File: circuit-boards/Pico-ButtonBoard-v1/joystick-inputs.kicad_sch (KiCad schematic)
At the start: 26 parts, among them J20 XY0-R, J21 XY1-L, U6 SN74LVC1G3157DBVR, U8 TLV77033DDC

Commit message: Update footprints
Signed-off-by: Scott Berman <sgberman1@gmail.com>
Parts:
- added TP301, TP302: CAN_RX, TestPoint:TestPoint_Keystone_5000-5004_Miniature, symbol Connector:TestPoint
- C301: renamed from C33; DIST (none) -> Digikey; DIST P/N (none) -> 445-4116-1-ND; MFG (none) -> TDK; MFG P/N (none) -> C2012X5R1E475K125AB
- C302: renamed from C27; value 1000pF-50V-10%-0805 -> 1000pF-50V-5%-0805; DIST (none) -> Digikey; DIST P/N (none) -> 399-C0805C102J5GACTUCT-ND; MFG (none) -> KEMET; MFG P/N (none) -> C0805C102J5GACTU
- C303: renamed from C25; value 1000pF-50V-10%-0805 -> 1000pF-50V-5%-0805; DIST (none) -> Digikey; DIST P/N (none) -> 399-C0805C102J5GACTUCT-ND; MFG (none) -> KEMET; MFG P/N (none) -> C0805C102J5GACTU
- C304: renamed from C28; value 1000pF-50V-10%-0805 -> 1000pF-50V-5%-0805; DIST (none) -> Digikey; DIST P/N (none) -> 399-C0805C102J5GACTUCT-ND; MFG (none) -> KEMET; MFG P/N (none) -> C0805C102J5GACTU
- C305: renamed from C26; value 1000pF-50V-10%-0805 -> 1000pF-50V-5%-0805; DIST (none) -> Digikey; DIST P/N (none) -> 399-C0805C102J5GACTUCT-ND; MFG (none) -> KEMET; MFG P/N (none) -> C0805C102J5GACTU
- C306: renamed from C31; DIST (none) -> Digikey; DIST P/N (none) -> 445-4116-1-ND; MFG (none) -> TDK; MFG P/N (none) -> C2012X5R1E475K125AB
- C309: renamed from C30; DIST (none) -> Digikey; DIST P/N (none) -> 445-4116-1-ND; MFG (none) -> TDK; MFG P/N (none) -> C2012X5R1E475K125AB
- C311: renamed from C37; value 1000pF-50V-10%-0805 -> 1000pF-50V-5%-0805; DIST (none) -> Digikey; DIST P/N (none) -> 399-C0805C102J5GACTUCT-ND; MFG (none) -> KEMET; MFG P/N (none) -> C0805C102J5GACTU
- R301: renamed from R55; DIST (none) -> Digikey; DIST P/N (none) -> 311-100KCRCT-ND; MFG (none) -> YAGEO; MFG P/N (none) -> RC0805FR-07100KL
- R302: renamed from R54; DIST (none) -> Digikey; DIST P/N (none) -> 311-100KCRCT-ND; MFG (none) -> YAGEO; MFG P/N (none) -> RC0805FR-07100KL
- R303: renamed from R56; DIST (none) -> Digikey; DIST P/N (none) -> 311-100KCRCT-ND; MFG (none) -> YAGEO; MFG P/N (none) -> RC0805FR-07100KL
- R304: renamed from R53; DIST (none) -> Digikey; DIST P/N (none) -> 311-100KCRCT-ND; MFG (none) -> YAGEO; MFG P/N (none) -> RC0805FR-07100KL
- R305: renamed from R57; value 49R9-1%-0805 -> 49.9R-1%-0805; DIST P/N 311-1.50KCRCT-ND -> RMCF0805FT49R9CT-ND; MFG YAGEO -> Stackpole; MFG P/N RC0805FR-071K5L -> RMCF0805FT49R9
- R306: renamed from R58; value 49R9-1%-0805 -> 49.9R-1%-0805; DIST P/N 311-1.50KCRCT-ND -> RMCF0805FT49R9CT-ND; MFG YAGEO -> Stackpole; MFG P/N RC0805FR-071K5L -> RMCF0805FT49R9
- R307: renamed from R51; value 49R9-1%-0805 -> 49.9R-1%-0805; DIST P/N 311-1.50KCRCT-ND -> RMCF0805FT49R9CT-ND; MFG YAGEO -> Stackpole; MFG P/N RC0805FR-071K5L -> RMCF0805FT49R9
- R308: renamed from R52; value 49R9-1%-0805 -> 49.9R-1%-0805; DIST P/N 311-1.50KCRCT-ND -> RMCF0805FT49R9CT-ND; MFG YAGEO -> Stackpole; MFG P/N RC0805FR-071K5L -> RMCF0805FT49R9
- R309: renamed from R50; DIST (none) -> Digikey; DIST P/N (none) -> 541-10.0KCCT-ND; MFG (none) -> Vishay Dale; MFG P/N (none) -> CRCW080510K0FKEA
- renumbered C32 to C307, C24 to C308, C29 to C310, J21 to J301, J20 to J302, L1 to L301, L2 to L302, U8 to U301, U6 to U302
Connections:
- net +3V3A: now also TP301.1
- net GNDA: now also TP302.1
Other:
- title: (none) -> Pico Button Board

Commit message: Pico Button Board initial placement
Signed-off-by: Scott Berman <sgberman1@gmail.com>
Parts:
- C307, C308, C310: LCSC Part # C519981 -> (none)

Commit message: Pico Button Board initial pcb checkin
Signed-off-by: Scott Berman <sgberman1@gmail.com>
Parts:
- removed L302: 10uH-10%-500mA-0805, Inductor_SMD:L_0805_2012Metric_Pad1.05x1.20mm_HandSolder, symbol Device:L_Small
- renumbered C302 to C10, C305 to C11, C301 to C16, C306 to C17, C309 to C18, C310 to C19, C308 to C21, C311 to C6, C307 to C7, C304 to C8, C303 to C9, J301 to J26, J302 to J27, L301 to L2, R309 to R28, R305 to R36, R306 to R37, R307 to R38, R308 to R39, R301 to R40, R303 to R41, R302 to R42, R304 to R43, TP301 to TP6, TP302 to TP7, U302 to U7, U301 to U9

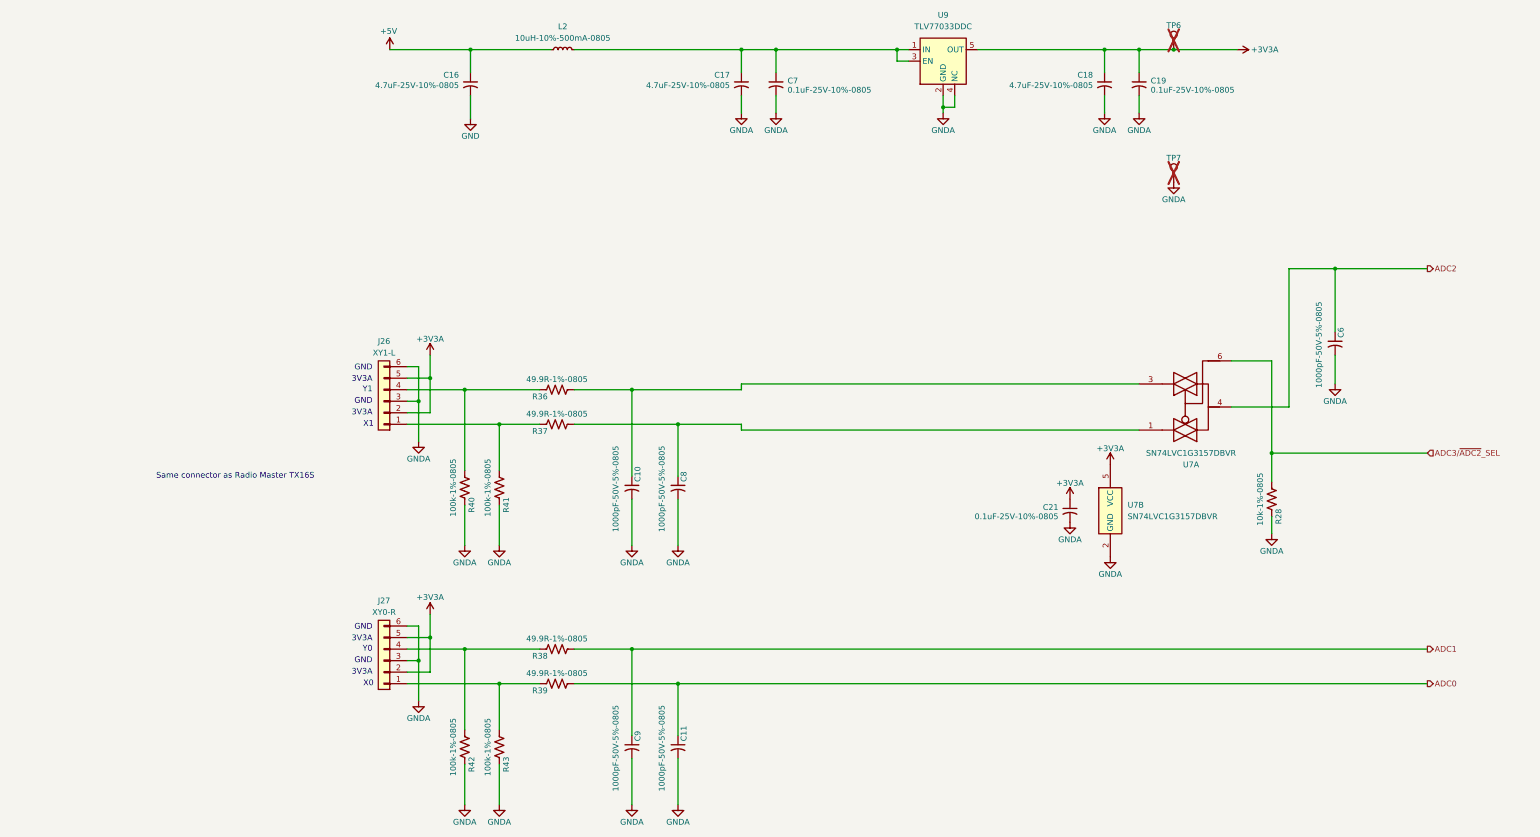
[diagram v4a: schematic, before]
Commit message: Changed button input circuit to use mux. Changed ADC3 to an external SPI ADC
Signed-off-by: Scott Berman <sgberman1@gmail.com>
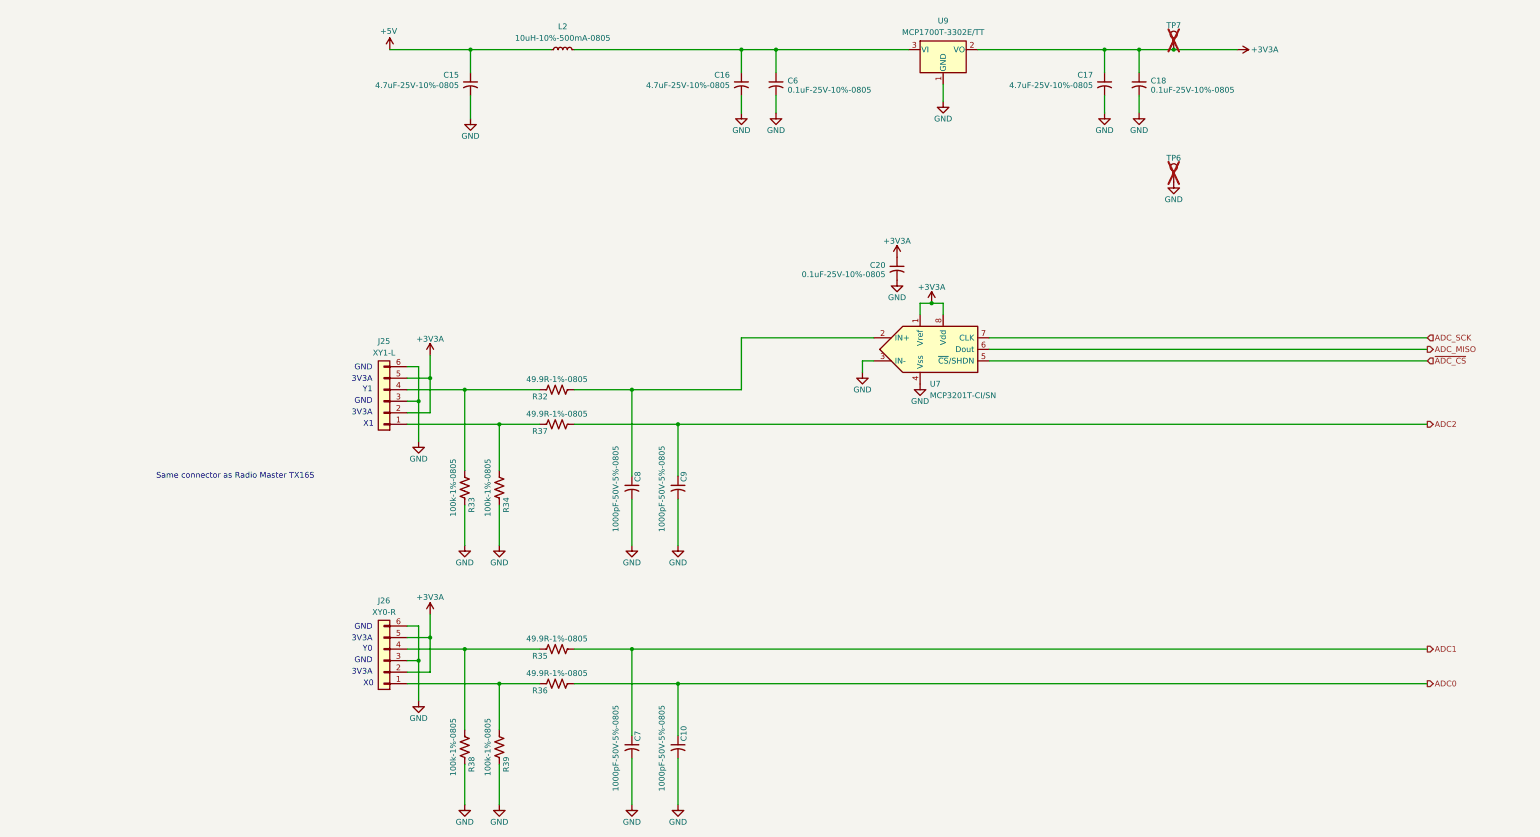
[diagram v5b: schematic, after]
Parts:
- removed C6: 1000pF-50V-5%-0805, Capacitor_SMD:C_0805_2012Metric_Pad1.18x1.45mm_HandSolder, symbol Device:C_Small_US
- removed R28: 10k-1%-0805, Resistor_SMD:R_0805_2012Metric_Pad1.20x1.40mm_HandSolder, symbol Device:R_US
- removed U7: SN74LVC1G3157DBVR, Package_TO_SOT_SMD:SOT-23-6_Handsoldering, symbol 74xGxx:74LVC1G3157
- removed U9: TLV77033DDC, Package_TO_SOT_SMD:SOT-23-5, symbol Pico-ButtonBoard:TLV77033DDC
- added U7: MCP3201T-CI/SN, Package_SO:SO-8_3.9x4.9mm_P1.27mm, symbol Analog_ADC:MCP3201
- added U9: MCP1700T-3302E/TT, Package_TO_SOT_SMD:SOT-23-3, symbol Regulator_Linear:MCP1700x-300xxTT
- renumbered C11 to C10, C16 to C15, C17 to C16, C18 to C17, C19 to C18, C21 to C20, C7 to C6, C9 to C7, C10 to C8, C8 to C9, J26 to J25, J27 to J26, R36 to R32, R40 to R33, R41 to R34, R38 to R35, R39 to R36, R42 to R38, R43 to R39, TP7 to TP6, TP6 to TP7
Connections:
- net GNDA is gone; now on net GND: C10.2, C16.2, C17.2, C18.2, C20.2, C6.2, C7.2, C8.2, C9.2, J25.3 (Pin_3), J25.6 (Pin_6), J26.3 (Pin_3), J26.6 (Pin_6), R33.1, R34.1, R38.1, R39.1, TP6.1
- net +3V3A: now also U7.1 (Vref), U7.8 (Vdd), U9.2 (VO)
- net ADC2: now also C9.1, R37.1
- net GND: now also U7.3 (IN-), U7.4 (Vss), U9.1 (GND)
- net at C16.1, C6.1, L2.2: now also U9.3 (VI)
- net at C8.1, R32.1: now also U7.2 (IN+)
- new net ADC_MISO: U7.6 (Dout)
- new net ADC_SCK: U7.7 (CLK)
- new net ~{ADC_CS}: U7.5 (~{CS}/SHDN)
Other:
- moved on the sheet: C20

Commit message: Add power over CAN to supply joystick from button interfaces.
Signed-off-by: Scott Berman <sgberman1@gmail.com>
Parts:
- TP4: renamed from TP6; value CAN_RX -> GND
- TP7: value CAN_RX -> 3V3A
- renumbered C15 to C13, C16 to C14, C17 to C15, C18 to C16, C20 to C18, C10 to C20, C9 to C21, C7 to C6, C8 to C7, C6 to C8, J26 to J25, J25 to J26, R35 to R24, R36 to R25, R37 to R26, R32 to R27, R38 to R45, R39 to R46, R34 to R47, R33 to R48
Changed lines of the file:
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@@
 	(title_block
 		(title "Pico Button Board")
-		(date "2025-12-29")
+		(date "2025-12-30")
 		(rev "1")
 	)
@@
 		(on_board yes)
 		(dnp no)
-		(property "Reference" "C18"
+		(property "Reference" "C16"
 			(at 279.4 77.978 0)
 			(effects
@@
 			(project "Pico-ButtonBoard-v1"
 				(path "/644201a9-3a2f-4df3-9c93-2ae55394df4b/685073ee-f919-44b0-8568-43a13e57da9c"
-					(reference "C18")
+					(reference "C16")
 					(unit 1)
 				)
@@
 			)
 		)
-		(property "Value" "CAN_RX"
+		(property "Value" "3V3A"
 			(at 287.02 69.0879 0)
 			(effects
@@
 		(on_board yes)
 		(dnp no)
-		(property "Reference" "J26"
+		(property "Reference" "J25"
 			(at 110.49 192.532 0)
 			(effects
@@
 			(project ""
 				(path "/644201a9-3a2f-4df3-9c93-2ae55394df4b/685073ee-f919-44b0-8568-43a13e57da9c"
-					(reference "J26")
+					(reference "J25")
 					(unit 1)
 				)
@@
 		(on_board yes)
 		(dnp no)
-		(property "Reference" "R36"
+		(property "Reference" "R25"
 			(at 146.558 212.344 90)
 			(effects
@@
 			(project "Pico-ButtonBoard-v1"
 				(path "/644201a9-3a2f-4df3-9c93-2ae55394df4b/685073ee-f919-44b0-8568-43a13e57da9c"
-					(reference "R36")
+					(reference "R25")
 					(unit 1)
 				)
@@
 		(on_board yes)
 		(dnp no)
-		(property "Reference" "R33"
+		(property "Reference" "R48"
 			(at 129.794 171.45 90)
 			(effects
@@
 			(project "Pico-ButtonBoard-v1"
 				(path "/644201a9-3a2f-4df3-9c93-2ae55394df4b/685073ee-f919-44b0-8568-43a13e57da9c"
-					(reference "R33")
+					(reference "R48")
 					(unit 1)
 				)
@@
 		(on_board yes)
 		(dnp no)
-		(property "Reference" "C7"
+		(property "Reference" "C6"
 			(at 166.37 223.52 90)
 			(effects
@@
 			(project "Pico-ButtonBoard-v1"
 				(path "/644201a9-3a2f-4df3-9c93-2ae55394df4b/685073ee-f919-44b0-8568-43a13e57da9c"
-					(reference "C7")
+					(reference "C6")
 					(unit 1)
 				)
@@
 		(on_board yes)
 		(dnp no)
-		(property "Reference" "C8"
+		(property "Reference" "C7"
 			(at 166.37 166.37 90)
 			(effects
@@
 			(project "Pico-ButtonBoard-v1"
 				(path "/644201a9-3a2f-4df3-9c93-2ae55394df4b/685073ee-f919-44b0-8568-43a13e57da9c"
-					(reference "C8")
+					(reference "C7")
 					(unit 1)
 				)
@@
 		(on_board yes)
 		(dnp no)
-		(property "Reference" "R32"
+		(property "Reference" "R27"
 			(at 146.558 147.574 90)
 			(effects
@@
 			(project "Pico-ButtonBoard-v1"
 				(path "/644201a9-3a2f-4df3-9c93-2ae55394df4b/685073ee-f919-44b0-8568-43a13e57da9c"
-					(reference "R32")
+					(reference "R27")
 					(unit 1)
 				)
@@
 		(on_board yes)
 		(dnp no)
-		(property "Reference" "R37"
+		(property "Reference" "R26"
 			(at 146.558 155.194 90)
 			(effects
@@
 			(project "Pico-ButtonBoard-v1"
 				(path "/644201a9-3a2f-4df3-9c93-2ae55394df4b/685073ee-f919-44b0-8568-43a13e57da9c"
-					(reference "R37")
+					(reference "R26")
 					(unit 1)
 				)
@@
 		(on_board yes)
 		(dnp no)
-		(property "Reference" "C20"
+		(property "Reference" "C18"
 			(at 220.98 118.618 0)
 			(effects
@@
 			(project "Pico-ButtonBoard-v1"
 				(path "/644201a9-3a2f-4df3-9c93-2ae55394df4b/685073ee-f919-44b0-8568-43a13e57da9c"
-					(reference "C20")
+					(reference "C18")
 					(unit 1)
 				)
@@
 		(on_board yes)
 		(dnp no)
-		(property "Reference" "C6"
+		(property "Reference" "C8"
 			(at 199.39 77.978 0)
 			(effects
@@
 			(project "Pico-ButtonBoard-v1"
 				(path "/644201a9-3a2f-4df3-9c93-2ae55394df4b/685073ee-f919-44b0-8568-43a13e57da9c"
-					(reference "C6")
+					(reference "C8")
 					(unit 1)
 				)
@@
 		(on_board yes)
 		(dnp no)
-		(property "Reference" "R39"
+		(property "Reference" "R46"
 			(at 137.414 228.6 90)
 			(effects
@@
 			(project "Pico-ButtonBoard-v1"
 				(path "/644201a9-3a2f-4df3-9c93-2ae55394df4b/685073ee-f919-44b0-8568-43a13e57da9c"
-					(reference "R39")
+					(reference "R46")
 					(unit 1)
 				)
@@
 		(on_board yes)
 		(dnp no)
-		(property "Reference" "C15"
+		(property "Reference" "C13"
 			(at 127 76.708 0)
 			(effects
@@
 			(project "Pico-ButtonBoard-v1"
 				(path "/644201a9-3a2f-4df3-9c93-2ae55394df4b/685073ee-f919-44b0-8568-43a13e57da9c"
-					(reference "C15")
+					(reference "C13")
 					(unit 1)
 				)
@@
 		(on_board yes)
 		(dnp yes)
-		(property "Reference" "TP6"
+		(property "Reference" "TP4"
 			(at 284.48 94.996 0)
 			(effects
@@
 			)
 		)
-		(property "Value" "CAN_RX"
+		(property "Value" "GND"
 			(at 287.02 98.2979 0)
 			(effects
@@
 			(project "Pico-ButtonBoard-v1"
 				(path "/644201a9-3a2f-4df3-9c93-2ae55394df4b/685073ee-f919-44b0-8568-43a13e57da9c"
-					(reference "TP6")
+					(reference "TP4")
 					(unit 1)
 				)
@@
 		(on_board yes)
 		(dnp no)
-		(property "Reference" "C10"
+		(property "Reference" "C20"
 			(at 176.53 223.52 90)
 			(effects
@@
 			(project "Pico-ButtonBoard-v1"
 				(path "/644201a9-3a2f-4df3-9c93-2ae55394df4b/685073ee-f919-44b0-8568-43a13e57da9c"
-					(reference "C10")
+					(reference "C20")
 					(unit 1)
 				)
@@
 		(on_board yes)
 		(dnp no)
-		(property "Reference" "R35"
+		(property "Reference" "R24"
 			(at 146.558 204.724 90)
 			(effects
@@
 			(project "Pico-ButtonBoard-v1"
 				(path "/644201a9-3a2f-4df3-9c93-2ae55394df4b/685073ee-f919-44b0-8568-43a13e57da9c"
-					(reference "R35")
+					(reference "R24")
 					(unit 1)
 				)
@@
 		(on_board yes)
 		(dnp no)
-		(property "Reference" "C16"
+		(property "Reference" "C14"
 			(at 186.69 76.708 0)
 			(effects
@@
 			(project "Pico-ButtonBoard-v1"
 				(path "/644201a9-3a2f-4df3-9c93-2ae55394df4b/685073ee-f919-44b0-8568-43a13e57da9c"
-					(reference "C16")
+					(reference "C14")
 					(unit 1)
 				)
@@
 		(on_board yes)
 		(dnp no)
-		(property "Reference" "C17"
+		(property "Reference" "C15"
 			(at 266.7 76.708 0)
 			(effects
@@
 			(project "Pico-ButtonBoard-v1"
 				(path "/644201a9-3a2f-4df3-9c93-2ae55394df4b/685073ee-f919-44b0-8568-43a13e57da9c"
-					(reference "C17")
+					(reference "C15")
 					(unit 1)
 				)
@@
 		(on_board yes)
 		(dnp no)
-		(property "Reference" "J25"
+		(property "Reference" "J26"
 			(at 110.49 135.382 0)
 			(effects
@@
 			(project "Pico-ButtonBoard-v1"
 				(path "/644201a9-3a2f-4df3-9c93-2ae55394df4b/685073ee-f919-44b0-8568-43a13e57da9c"
-					(reference "J25")
+					(reference "J26")
 					(unit 1)
 				)
@@
 		(on_board yes)
 		(dnp no)
-		(property "Reference" "R34"
+		(property "Reference" "R47"
 			(at 137.414 171.45 90)
 			(effects
@@
 			(project "Pico-ButtonBoard-v1"
 				(path "/644201a9-3a2f-4df3-9c93-2ae55394df4b/685073ee-f919-44b0-8568-43a13e57da9c"
-					(reference "R34")
+					(reference "R47")
 					(unit 1)
 				)
@@
 		(on_board yes)
 		(dnp no)
-		(property "Reference" "C9"
+		(property "Reference" "C21"
 			(at 176.53 166.37 90)
 			(effects
@@
 			(project "Pico-ButtonBoard-v1"
 				(path "/644201a9-3a2f-4df3-9c93-2ae55394df4b/685073ee-f919-44b0-8568-43a13e57da9c"
-					(reference "C9")
+					(reference "C21")
 					(unit 1)
 				)
@@
 		(on_board yes)
 		(dnp no)
-		(property "Reference" "R38"
+		(property "Reference" "R45"
 			(at 129.794 228.6 90)
 			(effects
@@
 			(project "Pico-ButtonBoard-v1"
 				(path "/644201a9-3a2f-4df3-9c93-2ae55394df4b/685073ee-f919-44b0-8568-43a13e57da9c"
-					(reference "R38")
+					(reference "R45")
 					(unit 1)
 				)

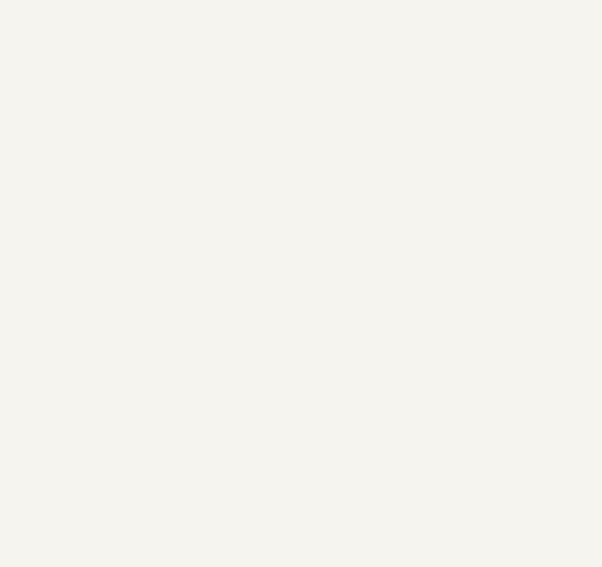
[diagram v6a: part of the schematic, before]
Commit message: Change diodes to schottky. Change 5V setpoint to 5.18V
Signed-off-by: Scott Berman <sgberman1@gmail.com>
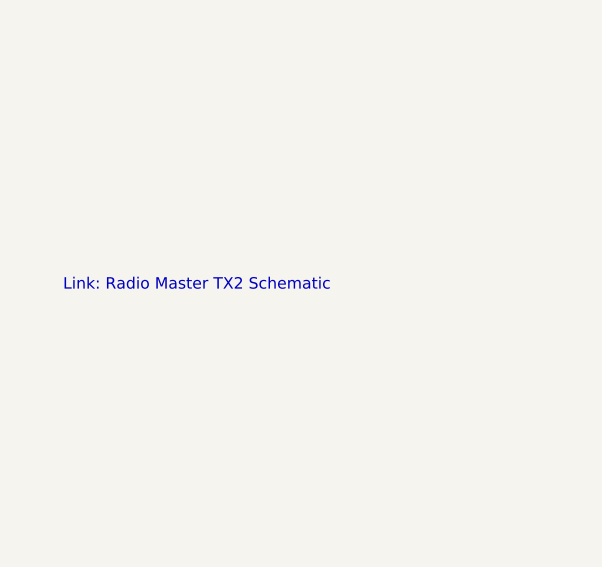
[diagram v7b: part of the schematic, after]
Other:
- note added: "Link: Radio Master TX2 Schematic"
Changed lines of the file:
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@@
 	(title_block
 		(title "Pico Button Board")
-		(date "2025-12-30")
+		(date "2025-12-31")
 		(rev "1")
 	)
@@
 		)
 	)
+	(text "Link: Radio Master TX2 Schematic"
+		(exclude_from_sim no)
+		(at 47.752 204.47 0)
+		(effects
+			(font
+				(size 1.27 1.27)
+			)
+			(href "https://www.rcgroups.com/forums/showthread.php?3869543-Blog-17-RadioMaster-TX16S-schematic-diagram")
+		)
+	)
